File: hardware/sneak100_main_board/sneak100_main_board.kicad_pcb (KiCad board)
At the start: 2 copper layers, 68 x 75 mm, 95 parts, among them J1 Conn_01x06, J10 Conn_01x06, J2 Conn_01x06, J3 Conn_01x06, J4 Conn_01x06, J5 Conn_01x02, J6 Conn_01x03, J7 Conn_01x03, J8 Conn_01x03, J9 Conn_01x03, Q1 AO4407, Q2 AO4407, Q3 SFH-313FA, Q4 SFH-313FA, Q5 SFH-313FA, Q6 SFH-313FA, SW1 SW_Push_SPDT, SW2 SW_Push, SW3 SW_Push, SW4 SW_Push, U1 DRV8835, U10 SSD1306, U11 TSOP4838, U2 DRV8835, U3 DRV8835, U4 DRV8835, U5 LM1117-3.3, U6 S9V11F5, U7 CD4051B, U8 CD4051B, U9 STM32F405RGTx, Y1 8MHz

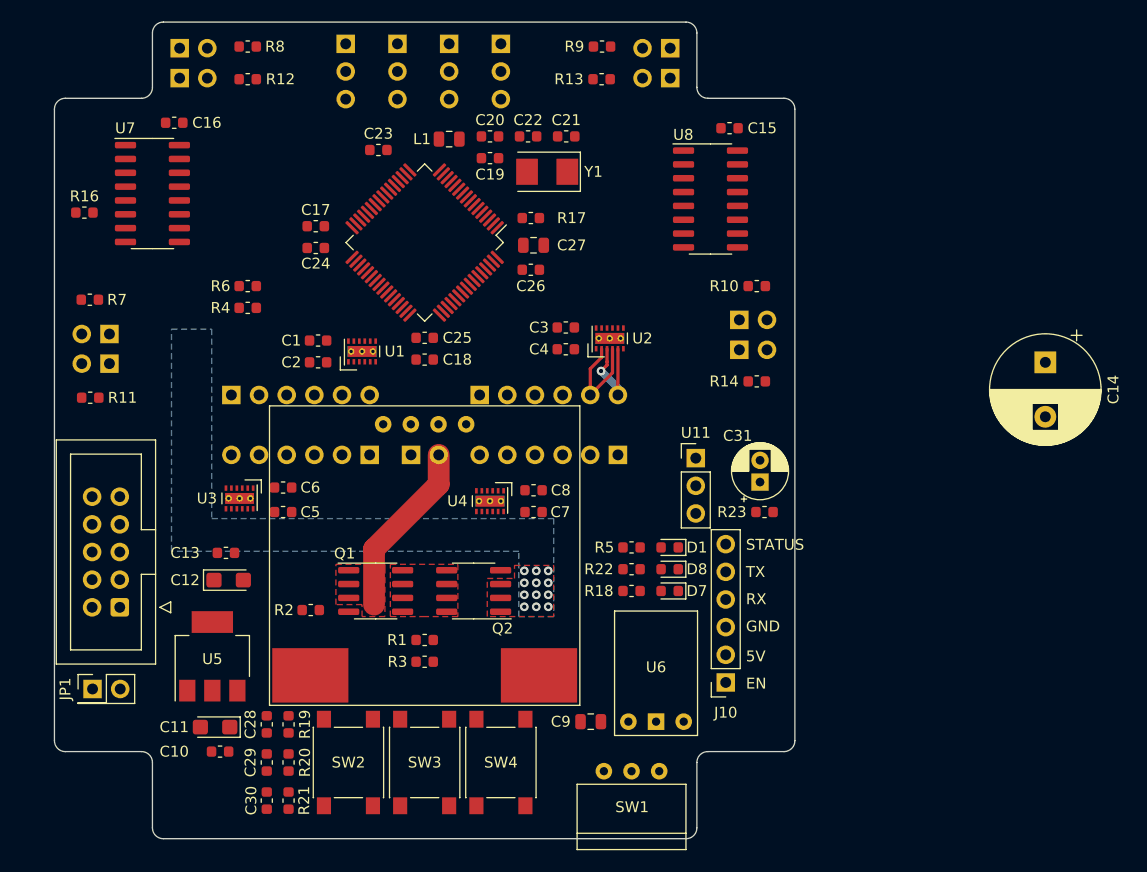
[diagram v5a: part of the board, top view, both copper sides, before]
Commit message: Add external proximity sensor, erase old from schematic
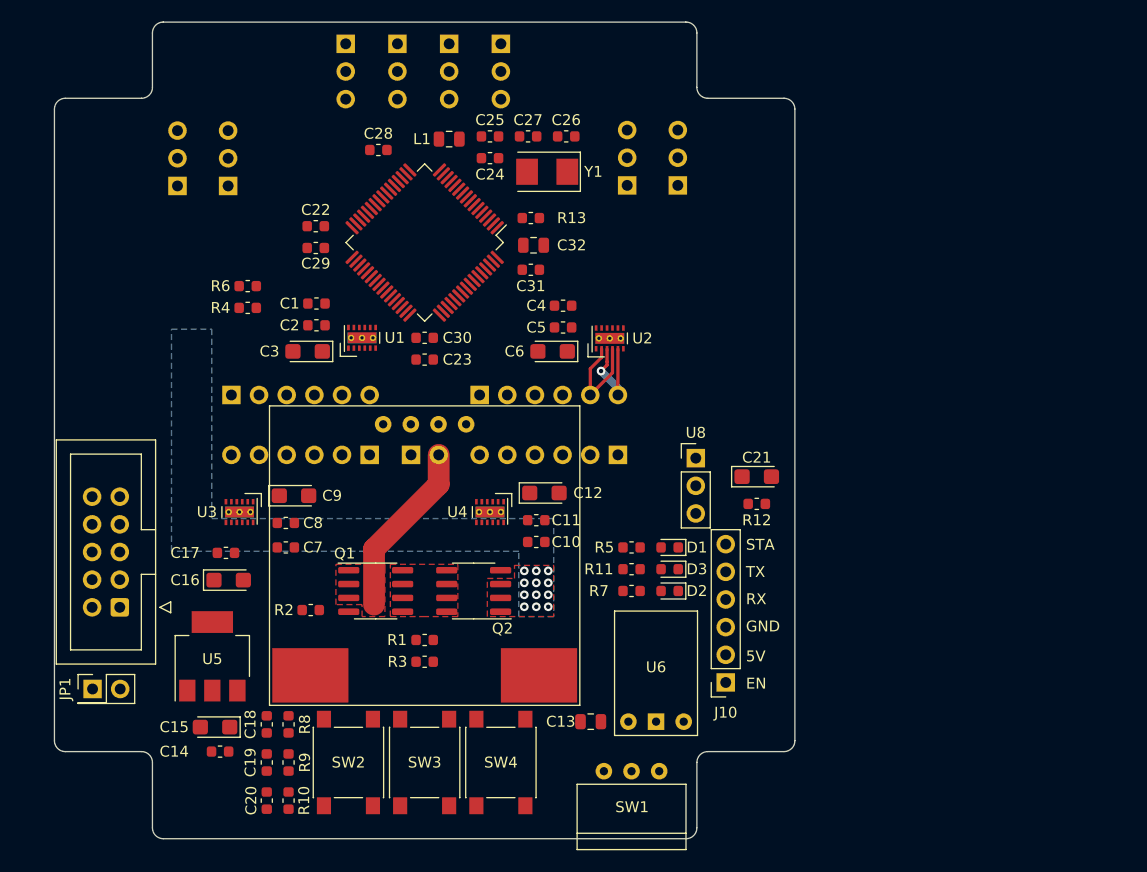
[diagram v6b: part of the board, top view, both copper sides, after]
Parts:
- removed the C14 at (204.8, 72.8)
- removed the C15 at (175.8, 51.2)
- removed the C16 at (124.8, 50.8)
- removed the D2 at (118.8, 72.9)
- removed the D3 at (125.2, 46.6)
- removed D4, D5: SFH4550, Connector_PinHeader_2.54mm:PinHeader_1x02_P2.54mm_Vertical
- removed Q3, Q4, Q5, Q6: SFH-313FA, Connector_PinHeader_2.54mm:PinHeader_1x02_P2.54mm_Vertical
- removed the R10 at (178.2, 65.8)
- removed the R11 at (117.0, 76.0)
- removed the R12 at (131.5, 46.8)
- removed the R13 at (164.0, 46.8)
- removed R14: 20, Resistor_SMD:R_0603_1608Metric
- removed R16: 4k7, Resistor_SMD:R_0603_1608Metric
- removed the R7 at (117.0, 67.0)
- removed the R8 at (131.5, 43.8)
- removed the R9 at (164.0, 43.8)
- removed the U7 at (122.8, 57.2)
- removed the U8 at (174.0, 57.8)
- added C12: 47uF, Capacitor_Tantalum_SMD:CP_EIA-3216-18_Kemet-A, F.Cu at (158.8, 84.8)
- added C3: 47uF, Capacitor_Tantalum_SMD:CP_EIA-3216-18_Kemet-A, F.Cu at (137.0, 71.8)
- added C6: 47uF, Capacitor_Tantalum_SMD:CP_EIA-3216-18_Kemet-A, F.Cu at (159.5, 71.8)
- added C9: 47uF, Capacitor_Tantalum_SMD:CP_EIA-3216-18_Kemet-A, F.Cu at (135.8, 85.0)
- added J11: Conn_01x03, Connector_PinHeader_2.54mm:PinHeader_1x03_P2.54mm_Vertical, B.Cu at (125.0, 56.5)
- added J12: Conn_01x03, Connector_PinHeader_2.54mm:PinHeader_1x03_P2.54mm_Vertical, B.Cu at (129.7, 56.5)
- added J13: Conn_01x03, Connector_PinHeader_2.54mm:PinHeader_1x03_P2.54mm_Vertical, B.Cu at (166.3, 56.5)
- added J14: Conn_01x03, Connector_PinHeader_2.54mm:PinHeader_1x03_P2.54mm_Vertical, B.Cu at (171.0, 56.5)
- C21: renamed from C31; footprint Capacitor_THT:CP_Radial_D5.0mm_P2.00mm -> Capacitor_Tantalum_SMD:CP_EIA-3216-18_Kemet-A
- R4: value 16k -> 18k
- moved C1 3.40 mm to (137.8, 67.3)
- moved C2 3.40 mm to (137.8, 69.3)
- moved C7 3.26 mm to (135.0, 89.8)
- moved C8 3.26 mm to (135.0, 87.5)
- moved C10 2.76 mm to (158.0, 89.2)
- moved C11 2.76 mm to (158.0, 87.2)
- moved C4 2.02 mm to (160.5, 67.5)
- moved C5 2.02 mm to (160.5, 69.5)
- moved U1 1.25 mm to (142.0, 70.5)
- moved U3 1.25 mm to (130.8, 86.5)
- moved R12 1.03 mm to (178.2, 85.8)
- moved U4 1.00 mm to (153.8, 86.5)
- moved C21 0.58 mm to (178.2, 83.2), turned to 0 degrees
- renumbered C7 to C10, C8 to C11, C9 to C13, C10 to C14, C11 to C15, C12 to C16, C13 to C17, C28 to C18, C29 to C19, C30 to C20, C17 to C22, C18 to C23, C19 to C24, C20 to C25, C21 to C26, C22 to C27, C23 to C28, C24 to C29, C25 to C30, C26 to C31, C27 to C32, C3 to C4, C4 to C5, C5 to C7, C6 to C8, D7 to D2, D8 to D3, R21 to R10, R22 to R11, R23 to R12, R17 to R13, R18 to R7, R19 to R8, R20 to R9, U10 to U7, U11 to U8
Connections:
- U9 pad 25: /controller/PROXIMITY_RX_READ -> /controller/PROXIMITY_RR
- U9 pad 39: /controller/PROXIMITY_TX_ENABLE -> (no net)
- U9 pad 55: /proximitySensors/ADD0 -> /controller/PROXIMITY_LL
- U9 pad 56: /proximitySensors/ADD1 -> /controller/PROXIMITY_FL
- U9 pad 57: /proximitySensors/ADD2 -> /controller/PROXIMITY_FR
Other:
- board text added: "STA"
- board text removed: "STATUS"

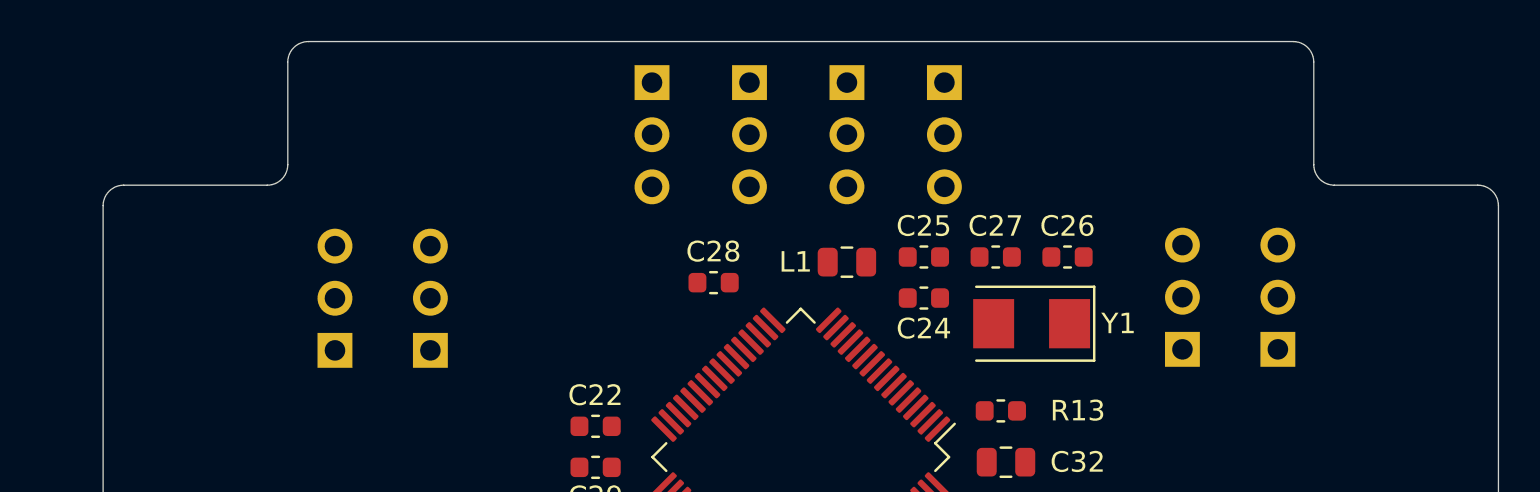
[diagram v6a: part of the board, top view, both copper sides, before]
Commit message: Hull with external proximity sensors
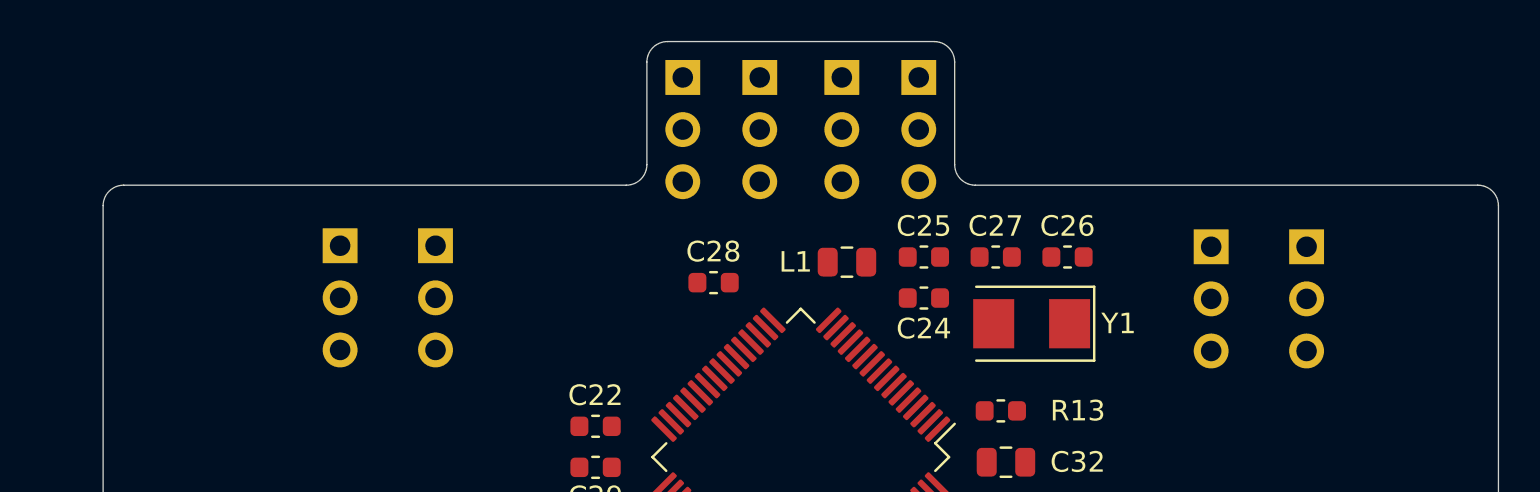
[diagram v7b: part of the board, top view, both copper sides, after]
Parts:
- moved J13 7.85 mm to (172.4, 51.5), turned to 180 degrees
- moved J11 7.07 mm to (129.9, 51.5), turned to 180 degrees
- moved J12 6.74 mm to (125.3, 51.5), turned to 180 degrees
- moved J14 5.96 mm to (167.8, 51.5), turned to 180 degrees
- moved J6 1.52 mm to (142.0, 43.2)
- moved J9 1.27 mm to (153.5, 43.2)
- moved J7 0.56 mm to (145.8, 43.2)
- moved J8 0.35 mm to (149.8, 43.2)
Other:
- outline, holes or cut-outs redrawn

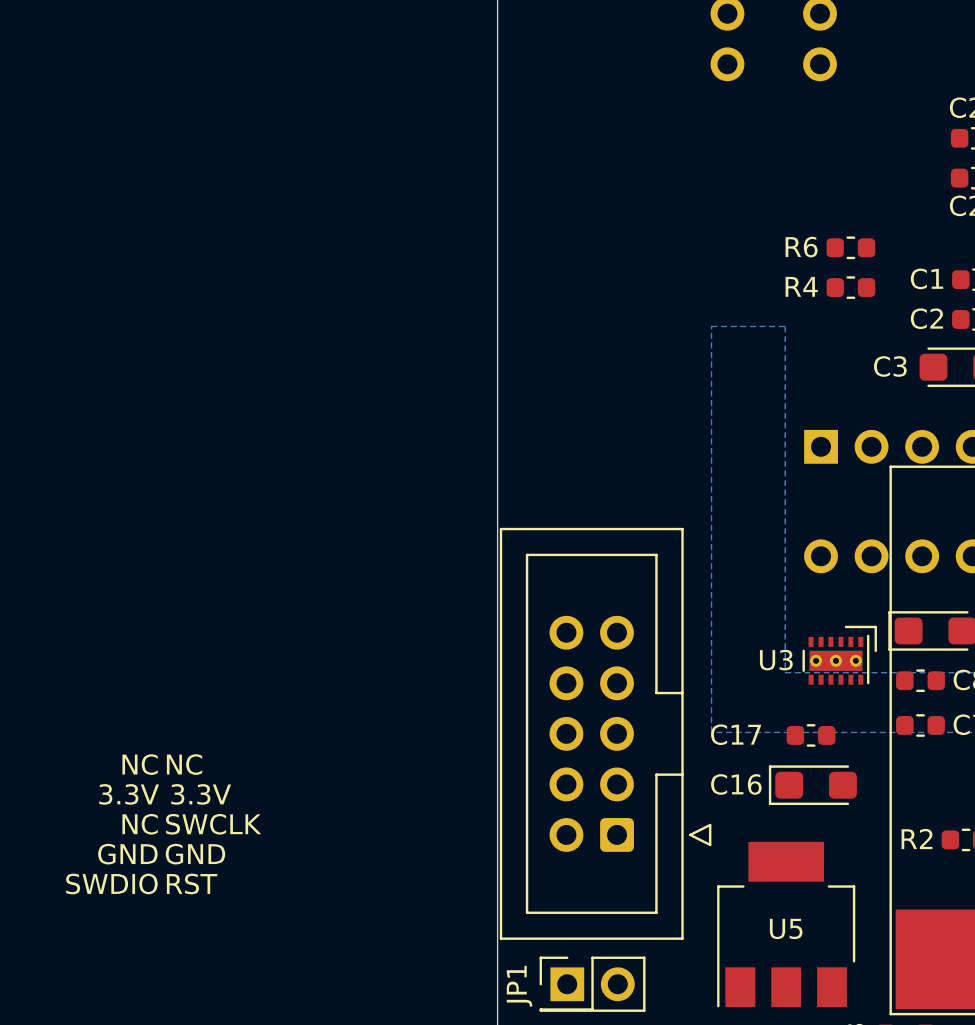
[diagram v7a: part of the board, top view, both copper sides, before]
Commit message: line sensors connectors
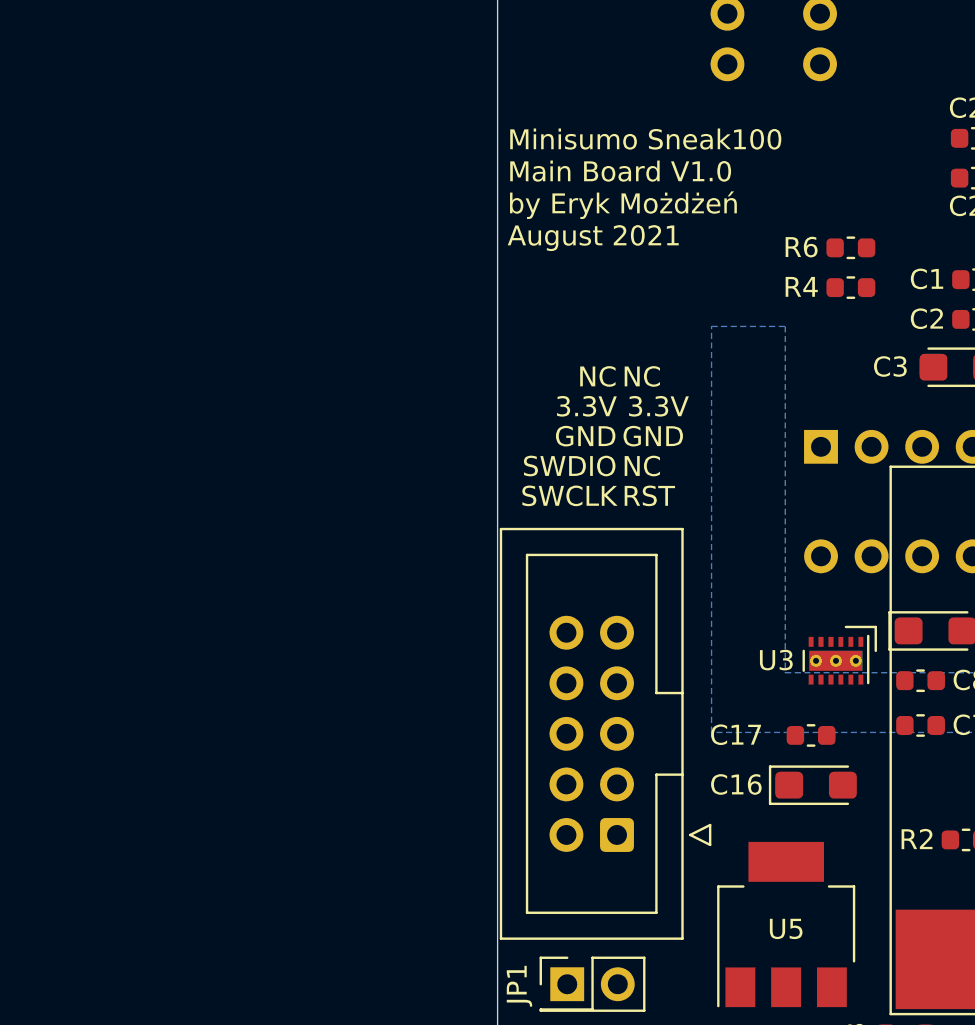
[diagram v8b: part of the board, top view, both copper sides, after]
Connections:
- MCU1 pad 2: /controller/SWDIO -> /controller/SWCLK
- MCU1 pad 3: GND -> (no net)
- MCU1 pad 4: GND -> /controller/SWDIO
- MCU1 pad 5: (no net) -> GND
- MCU1 pad 6: /controller/SWCLK -> GND
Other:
- board text added: "Minisumo Sneak100 Main Board V1.0 by Eryk Możdżeń August 2021"
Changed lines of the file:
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@@
   (general
     (thickness 1.6)
-    (drawings 51)
+    (drawings 52)
     (tracks 28)
     (zones 0)
@@
     (add_net "Net-(J5-Pad2)")
     (add_net "Net-(MCU1-Pad10)")
-    (add_net "Net-(MCU1-Pad5)")
+    (add_net "Net-(MCU1-Pad3)")
     (add_net "Net-(MCU1-Pad9)")
     (add_net "Net-(Q1-Pad4)")
@@
       (net 47 ST-LINK_3.3V))
     (pad 6 thru_hole circle (at 2.54 5.08 180) (size 1.7 1.7) (drill 1) (layers *.Cu *.Mask)
-      (net 15 /controller/SWCLK))
-    (pad 4 thru_hole circle (at 2.54 2.54 180) (size 1.7 1.7) (drill 1) (layers *.Cu *.Mask)
       (net 1 GND))
-    (pad 2 thru_hole circle (at 2.54 0 180) (size 1.7 1.7) (drill 1) (layers *.Cu *.Mask)
+    (pad 4 thru_hole circle (at 2.54 2.54 180) (size 1.7 1.7) (drill 1) (layers *.Cu *.Mask)
       (net 16 /controller/SWDIO))
+    (pad 2 thru_hole circle (at 2.54 0 180) (size 1.7 1.7) (drill 1) (layers *.Cu *.Mask)
+      (net 15 /controller/SWCLK))
     (pad 9 thru_hole circle (at 0 10.16 180) (size 1.7 1.7) (drill 1) (layers *.Cu *.Mask))
     (pad 7 thru_hole circle (at 0 7.62 180) (size 1.7 1.7) (drill 1) (layers *.Cu *.Mask)
       (net 47 ST-LINK_3.3V))
-    (pad 5 thru_hole circle (at 0 5.08 180) (size 1.7 1.7) (drill 1) (layers *.Cu *.Mask))
-    (pad 3 thru_hole circle (at 0 2.54 180) (size 1.7 1.7) (drill 1) (layers *.Cu *.Mask)
+    (pad 5 thru_hole circle (at 0 5.08 180) (size 1.7 1.7) (drill 1) (layers *.Cu *.Mask)
       (net 1 GND))
+    (pad 3 thru_hole circle (at 0 2.54 180) (size 1.7 1.7) (drill 1) (layers *.Cu *.Mask))
     (pad 1 thru_hole roundrect (at 0 0 180) (size 1.7 1.7) (drill 1) (layers *.Cu *.Mask) (roundrect_rratio 0.147059)
       (net 46 /controller/RST))
@@
     )
   )
+  (gr_text "Minisumo Sneak100\nMain Board V1.0\nby Eryk Możdżeń\nAugust 2021" (at 114.25 62.75) (layer F.SilkS)
+    (effects (font (size 1 1) (thickness 0.15)) (justify left))
+  )
   (dimension 25 (width 0.15) (layer Dwgs.User)
     (gr_text "25.000 mm" (at 135.25 35.95) (layer Dwgs.User)
@@
     (effects (font (size 1 1) (thickness 0.15)) (justify left))
   )
-  (gr_text NC (at 96.75 91.75) (layer F.SilkS)
+  (gr_text NC (at 119.75 72.25) (layer F.SilkS)
     (effects (font (size 1 1) (thickness 0.15)) (justify right))
   )
-  (gr_text NC (at 97 91.75) (layer F.SilkS)
+  (gr_text NC (at 120 72.25) (layer F.SilkS)
     (effects (font (size 1 1) (thickness 0.15)) (justify left))
   )
-  (gr_text 3.3V (at 97.25 93.25) (layer F.SilkS)
+  (gr_text 3.3V (at 120.25 73.75) (layer F.SilkS)
     (effects (font (size 1 1) (thickness 0.15)) (justify left))
   )
-  (gr_text 3.3V (at 96.75 93.25) (layer F.SilkS)
+  (gr_text 3.3V (at 119.75 73.75) (layer F.SilkS)
     (effects (font (size 1 1) (thickness 0.15)) (justify right))
   )
-  (gr_text SWCLK (at 97 94.75) (layer F.SilkS)
-    (effects (font (size 1 1) (thickness 0.15)) (justify left))
-  )
-  (gr_text NC (at 96.75 94.75) (layer F.SilkS)
+  (gr_text SWCLK (at 119.75 78.25) (layer F.SilkS)
     (effects (font (size 1 1) (thickness 0.15)) (justify right))
   )
-  (gr_text GND (at 97 96.25) (layer F.SilkS)
+  (gr_text NC (at 120 76.75) (layer F.SilkS)
+    (effects (font (size 1 1) (thickness 0.15)) (justify left))
+  )
+  (gr_text GND (at 120 75.25) (layer F.SilkS)
     (effects (font (size 1 1) (thickness 0.15)) (justify left))
   )
-  (gr_text GND (at 96.75 96.25) (layer F.SilkS)
+  (gr_text GND (at 119.75 75.25) (layer F.SilkS)
     (effects (font (size 1 1) (thickness 0.15)) (justify right))
   )
-  (gr_text SWDIO (at 96.75 97.75) (layer F.SilkS)
+  (gr_text SWDIO (at 119.75 76.75) (layer F.SilkS)
     (effects (font (size 1 1) (thickness 0.15)) (justify right))
   )
-  (gr_text RST (at 97 97.75) (layer F.SilkS)
+  (gr_text RST (at 120 78.25) (layer F.SilkS)
     (effects (font (size 1 1) (thickness 0.15)) (justify left))
   )
